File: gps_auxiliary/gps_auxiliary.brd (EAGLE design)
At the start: 61 x 59 mm, 5 parts, among them J1 FAN, J2 GPS, J3 2X6 FEMALE, U1 PYB10-Q24-S3

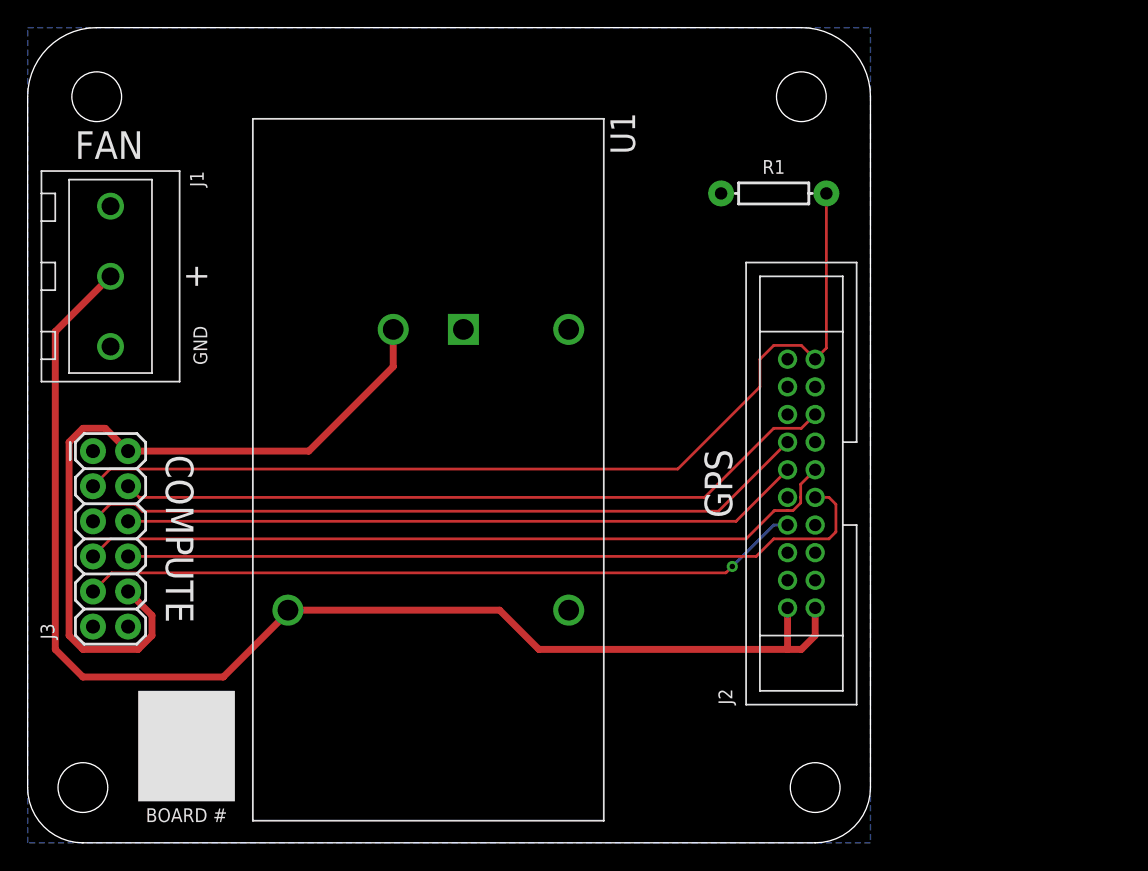
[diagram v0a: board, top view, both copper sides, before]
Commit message: Changed board dimensions to fit existing
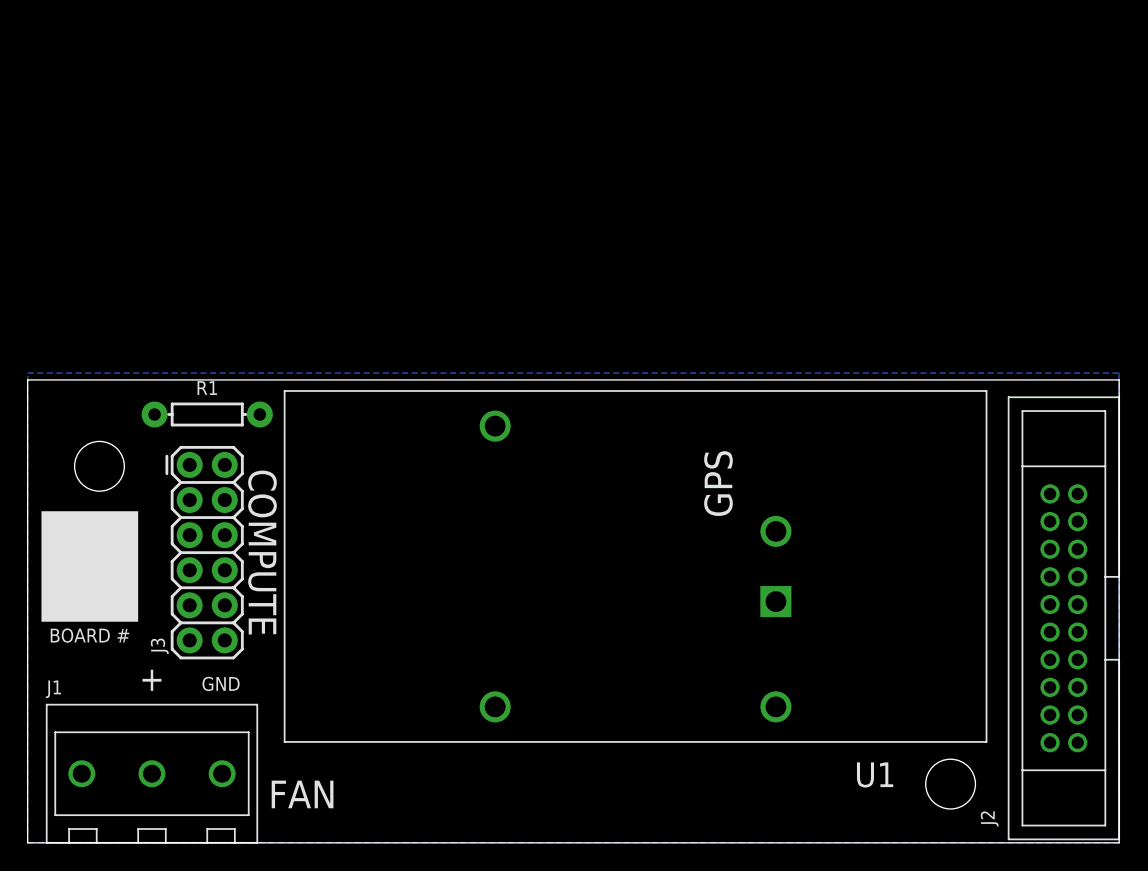
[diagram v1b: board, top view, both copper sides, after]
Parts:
- moved R1 44.0 mm to (13.0, 31.0)
- moved J1 36.1 mm to (9.00, 5.00), turned to 0 degrees
- moved J2 21.4 mm to (75.0, 16.2)
- moved U1 16.6 mm to (44.0, 20.0), turned to 180 degrees
- moved J3 7.07 mm to (13.0, 21.0)
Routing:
- net +3V3: track 93.2 -> 0.00 mm
- net PPS: track 70.4 -> 0.00 mm
- net PDTX: track 55.7 -> 0.00 mm
- net PATX: track 55.7 -> 0.00 mm
- net V+: track 54.5 -> 0.00 mm
- net PBTX: track 53.1 -> 0.00 mm
- net PBRX: track 52.6 -> 0.00 mm
- net PDRX: track 52.3 -> 0.00 mm, vias 1 -> 0
- net PARX: track 49.3 -> 0.00 mm
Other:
- board size 61 x 59 mm -> 79 x 33.5 mm

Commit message: Added capacitor to library and board
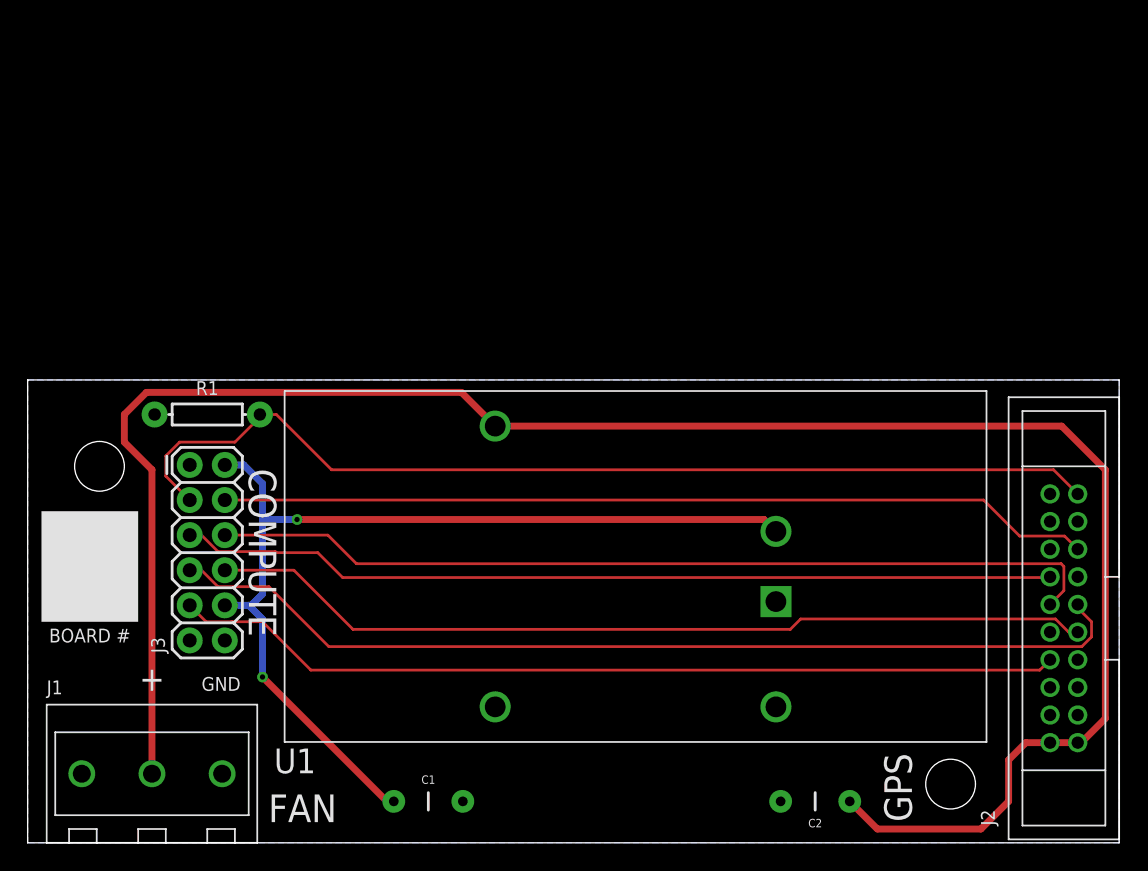
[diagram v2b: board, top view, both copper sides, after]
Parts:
- added C1, C2: 10uF 50V, gps_auxiliary:CAP-PTH-5MM
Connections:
- net +3V3: now also C2.1
- net GND: now also C1.2, C2.2
- net V+: now also C1.1
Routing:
- net +3V3: track 0.00 -> 143.2 mm
- net PPS: track 0.00 -> 73.6 mm
- net V+: track 0.00 -> 70.9 mm, vias 0 -> 2
- net PATX: track 0.00 -> 70.6 mm
- net PARX: track 0.00 -> 64.8 mm
- net PDRX: track 0.00 -> 64.5 mm
- net PDTX: track 0.00 -> 64.2 mm
- net PBTX: track 0.00 -> 63.6 mm
- net PBRX: track 0.00 -> 63.2 mm
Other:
- board text added: "AutoRally GPS Interface v 1.1 Sept. 2019"
- board text removed: "AutoRally GPS Interface v 1.0 Sept. 2019"
